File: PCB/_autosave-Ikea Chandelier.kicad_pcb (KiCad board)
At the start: 2 copper layers, 50 x 50 mm, 23 parts, among them J1 Arduino Pro Mini, P1 RGB12, P2 Power, P3 RGB34, P4 RS485, P5 RGB56, P6 Candles, U1 78L05, U2 MAX485

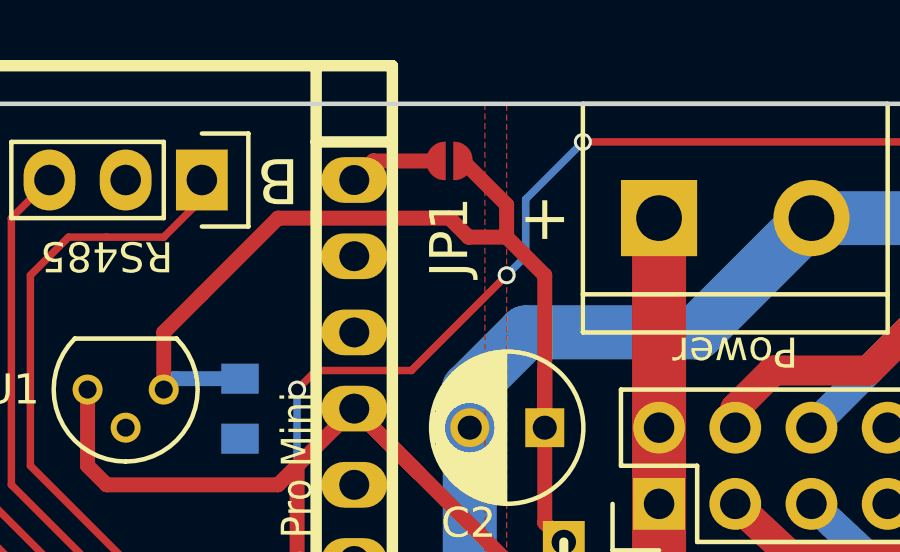
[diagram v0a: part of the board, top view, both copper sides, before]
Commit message: Diode corrected, markings fixed, ordered v1
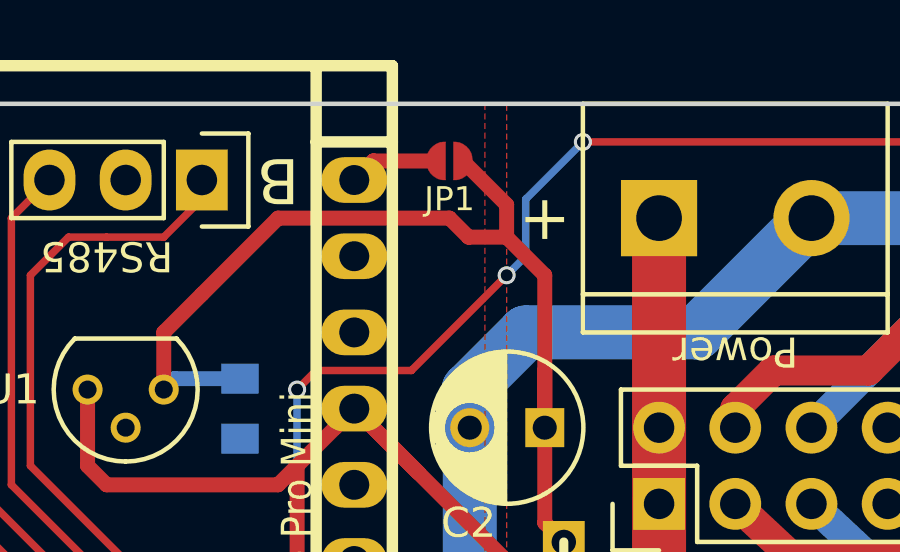
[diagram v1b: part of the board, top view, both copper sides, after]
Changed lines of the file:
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@@
   (page A4)
   (layers
-    (0 F.Cu signal hide)
-    (31 B.Cu signal hide)
+    (0 F.Cu signal)
+    (31 B.Cu signal)
     (32 B.Adhes user)
     (33 F.Adhes user)
@@
     (pcbplotparams
       (layerselection 0x010f0_80000001)
-      (usegerberextensions false)
+      (usegerberextensions true)
       (excludeedgelayer true)
       (linewidth 0.100000)
@@
   (module septillion_device:SMD_jumper2 (layer F.Cu)
     (at 90.32 81.905)
-    (fp_text reference JP1 (at 0 2.54 90) (layer F.SilkS)
-      (effects (font (thickness 0.3)))
+    (fp_text reference JP1 (at 0 1.27 180) (layer F.SilkS)
+      (effects (font (size 0.8 0.8) (thickness 0.15)))
     )
     (fp_text value Jumper_NC_Small (at 3.556 6.096) (layer F.SilkS) hide
